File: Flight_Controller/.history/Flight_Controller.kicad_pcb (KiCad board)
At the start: 2 copper layers, 77 parts, among them IC1 AT7456E, J10 USB_C_Receptacle_USB2.0_16P, J11 Conn_ARM_SWD_TagConnect_TC203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, J13 SM06B-GHS-TB, J14 VTX, J6 ESC->FC DSHOT and Telem, J7 ELRS Reciever, J9 Camera, SW1 SW_Push, U1 STM32H743VITx, U2 BMI270, U3 TLV75533PDBV, U4 W25Q128JVSIQ TR, U5 TPS62932, U7 TPD2EUSB30ADRTR, Y2 ABM3-27.000MHZ-D2Y-T

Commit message: Initial Layout Done
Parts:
- removed C10: 33nF, PCM_JLCPCB:C_0603
- removed C12: 6.8pF, PCM_JLCPCB:C_0603
- removed U5: TPS62932, Package_TO_SOT_SMD:SOT-583-8
- added C34: 47uF, PCM_JLCPCB:C_0805, F.Cu at (104.9, 78.5)
- added D6: SMBJ30CA, PCM_JLCPCB:D_SMB, F.Cu at (123.3, 77.5)
- added H1: MountingHole, MountingHole:MountingHole_3.2mm_M3_Pad_Via, F.Cu at (97.4, 53.6)
- added H2: MountingHole, MountingHole:MountingHole_3.2mm_M3_Pad_Via, F.Cu at (127.4, 53.6)
- added H3: MountingHole, MountingHole:MountingHole_3.2mm_M3_Pad_Via, F.Cu at (97.4, 83.6)
- added H4: MountingHole, MountingHole:MountingHole_3.2mm_M3_Pad_Via, F.Cu at (127.4, 83.6)
- added U6: LMR51625XDDCR, Flight_Controller:DDC0006A-MFG, F.Cu at (118.3, 82.1)
- NT1, NT2, NT3, NT4: footprint NetTie:NetTie-2_THT_Pad1.0mm -> NetTie:NetTie-2_SMD_Pad0.5mm
- R7: value 52.3K -> 100kΩ
- R8: value 10kΩ -> 20kΩ
- moved J13 42.5 mm to (121.4, 47.0), turned to 180 degrees
- moved R16 37.3 mm to (122.8, 88.3), turned to 90 degrees
- moved R17 35.4 mm to (96.1, 88.8), turned to -90 degrees
- moved D4 35.3 mm to (120.7, 88.2)
- moved D5 33.4 mm to (98.4, 88.7)
- moved C33 32.8 mm to (121.3, 84.5)
- moved C7 32.4 mm to (123.0, 84.4)
- moved NT1 31.8 mm to (103.0, 52.7), turned to 90 degrees
- moved R5 31.5 mm to (104.8, 55.9), turned to 180 degrees
- moved C17 29.4 mm to (99.9, 88.4)
- moved R4 29.1 mm to (104.8, 54.5), turned to 180 degrees
- moved C2 28.3 mm to (107.7, 57.6), turned to 180 degrees
- moved NT3 27.6 mm to (105.2, 52.6), turned to 90 degrees
- moved J7 27.3 mm to (95.0, 74.5), turned to -90 degrees
- moved C3 26.5 mm to (107.7, 56.2), turned to 180 degrees
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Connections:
- net /Peripherals/Power/3V3_LED renamed /Peripherals/Power/BATT_LED
- net Net-(D1-Pad1) renamed /MCU/Connectors/MCU_LED
- net Net-(D2-Pad1) renamed /MCU/Connectors/USB_LED
- C11 pad 1: /Peripherals/Power/BST -> /Peripherals/Power/CB
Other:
- board outline added: 43.6 x 50 mm

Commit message: Updated Connector Standard
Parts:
- removed D1: Red, PCM_JLCPCB:D_0603
- removed R9: 150Ω, PCM_JLCPCB:R_0603
- added D8: Red, PCM_JLCPCB:D_0603, F.Cu at (127.5, 77.7)
- added R19: 150Ω, PCM_JLCPCB:R_0603, F.Cu at (131.0, 77.7)
- J11: moved to B.Cu
- moved C17 16.0 mm to (101.2, 72.5), turned to 180 degrees
- moved D5 13.6 mm to (101.2, 75.4), turned to 0 degrees
- moved R17 12.2 mm to (99.6, 77.1), turned to 0 degrees
- moved J11 11.0 mm to (123.7, 54.4), turned to 90 degrees
- moved R13 10.8 mm to (94.9, 55.4)
- moved C15 9.54 mm to (102.0, 77.8)
- moved C14 5.17 mm to (104.7, 88.6), turned to 180 degrees
- moved R16 5.00 mm to (127.7, 87.5), turned to 0 degrees
- moved R14 4.64 mm to (98.1, 46.5)
- moved C34 4.36 mm to (104.5, 82.8)
- moved C13 4.29 mm to (104.5, 85.0)
- moved U3 4.28 mm to (104.5, 79.5), turned to 90 degrees
- moved C27 4.06 mm to (100.8, 47.5)
- moved SW1 3.82 mm to (100.7, 45.6)
- moved R8 3.75 mm to (107.5, 78.8), turned to 90 degrees
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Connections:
- J6 pad 7: +BATT -> GND
- J6 pad 8: GND -> +BATT
- U1 pad 46: unconnected-(U1-PB10-Pad46) -> /MCU/Connectors/PB10
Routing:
- added copper zone on F.Cu, net +3V3
- added copper zone on F.Cu, net +5V
- added copper zone on F.Cu, net +BATT
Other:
- board size 43.6 x 50 mm -> 42 x 46 mm
- copper layers 2 -> 4

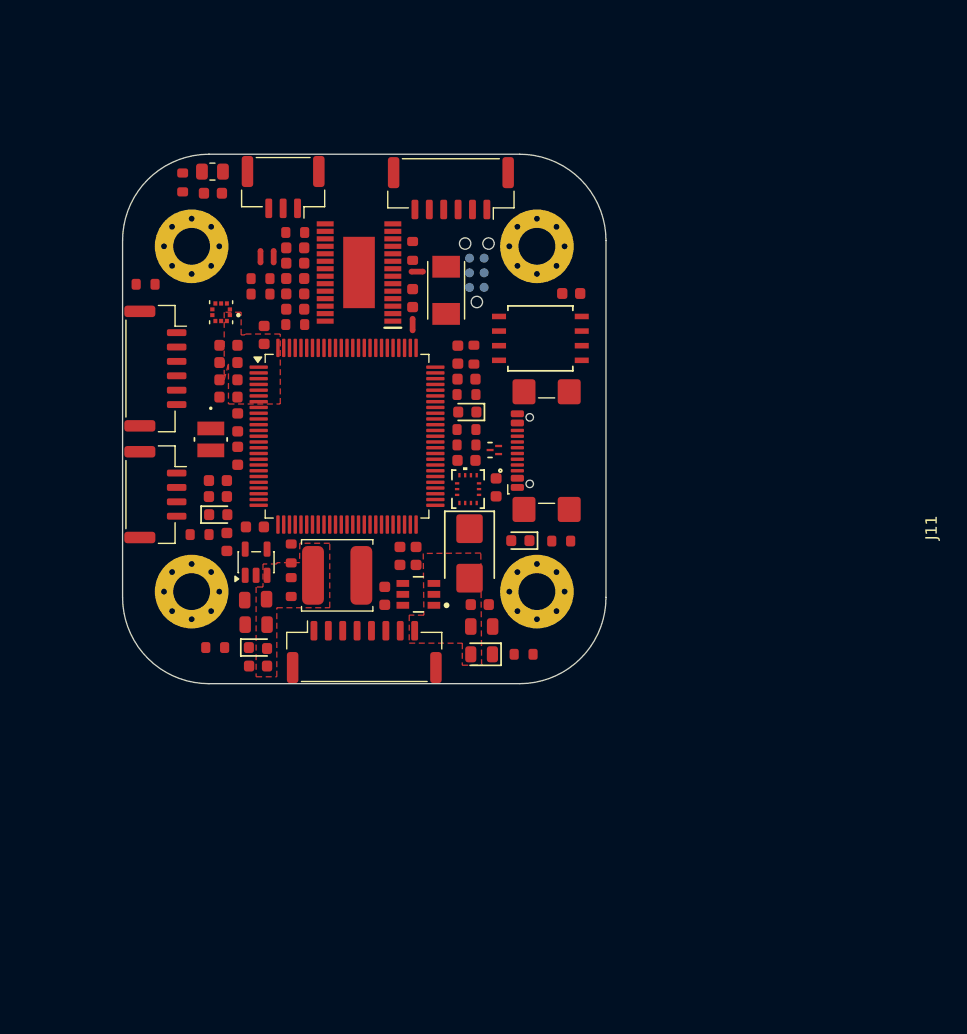
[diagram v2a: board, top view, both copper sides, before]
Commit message: Updated Layout to 60x30
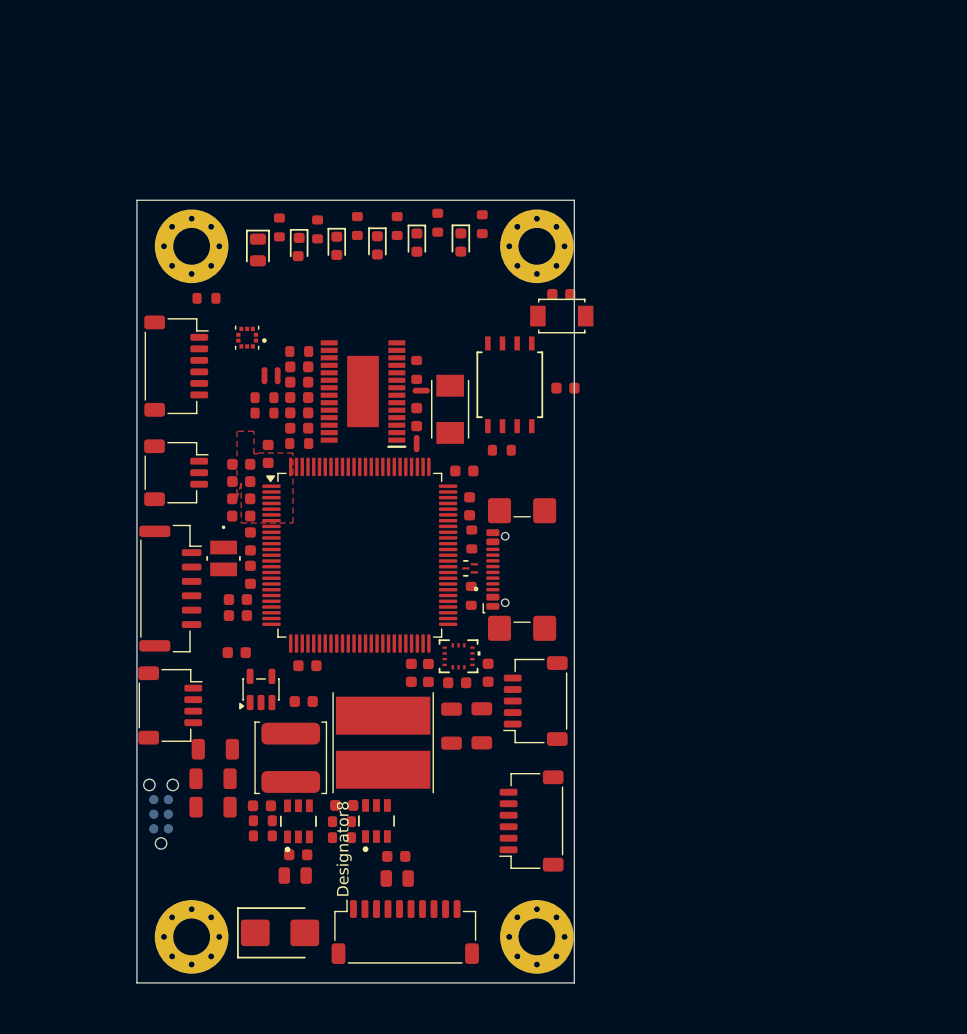
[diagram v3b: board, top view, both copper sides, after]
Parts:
- removed J14: VTX, Connector_JST:JST_GH_SM06B-GHS-TB_1x06-1MP_P1.25mm_Horizontal
- removed J6: ESC->FC DSHOT and Telem, Connector_JST:JST_GH_SM08B-GHS-TB_1x08-1MP_P1.25mm_Horizontal
- added C10: 100nF, PCM_JLCPCB:C_0603, F.Cu at (116.7, 105.1)
- added C12: 100nF, PCM_JLCPCB:C_0603, F.Cu at (112.2, 100.7)
- added C35: 22uF, PCM_JLCPCB:C_1206, F.Cu at (101.0, 95.8)
- added C36: 22uF, PCM_JLCPCB:C_1206, F.Cu at (124.1, 93.8)
- added C37: 22uF, PCM_JLCPCB:C_1206, F.Cu at (121.5, 93.8)
- added C5: 2.2uF, PCM_JLCPCB:C_0805, F.Cu at (116.8, 107.0)
- added D10: White, PCM_JLCPCB:D_0603, F.Cu at (111.5, 52.1)
- added J1: Analog VTX, Connector_JST:JST_SH_SM05B-SRSS-TB_1x05-1MP_P1.00mm_Horizontal, F.Cu at (128.8, 91.6)
- added J2: Digital VTX, Connector_JST:JST_SH_SM06B-SRSS-TB_1x06-1MP_P1.00mm_Horizontal, F.Cu at (128.4, 102.0)
- added J3: GPS+Mag, Connector_JST:JST_SH_SM06B-SRSS-TB_1x06-1MP_P1.00mm_Horizontal, F.Cu at (97.6, 62.5)
- added J4: ESC Connector, Connector_JST:JST_SH_SM10B-SRSS-TB_1x10-1MP_P1.00mm_Horizontal, F.Cu at (117.5, 111.7)
- added L2: 18uH, Inductor_SMD:L_TDK_VLP8040, F.Cu at (115.5, 95.2)
- added R18: 820Ω, PCM_JLCPCB:R_0603, F.Cu at (113.3, 50.3)
- added R9: 100kΩ, PCM_JLCPCB:R_0603, F.Cu at (112.0, 102.1)
- added U8: LMR51625XDDCR, Flight_Controller:DDC0006A-MFG, F.Cu at (115.0, 102.0)
- C13, C34: value 47uF -> 22uF; footprint PCM_JLCPCB:C_0805 -> PCM_JLCPCB:C_1206
- J7: footprint Connector_JST:JST_GH_SM04B-GHS-TB_1x04-1MP_P1.25mm_Horizontal -> Connector_JST:JST_SH_SM04B-SRSS-TB_1x04-1MP_P1.00mm_Horizontal
- J9: footprint Connector_JST:JST_GH_SM03B-GHS-TB_1x03-1MP_P1.25mm_Horizontal -> Connector_JST:JST_SH_SM03B-SRSS-TB_1x03-1MP_P1.00mm_Horizontal
- SW1: footprint Resistor_SMD:R_0805_2012Metric -> Flight_Controller:SW_TS-1088-AR02016
- moved R14 58.6 mm to (112.0, 103.5), turned to 180 degrees
- moved J11 54.5 mm to (96.2, 101.4)
- moved R16 42.7 mm to (106.5, 50.5), turned to 90 degrees
- moved J13 42.5 mm to (97.0, 81.8), turned to -90 degrees
- moved D4 40.1 mm to (104.7, 52.4), turned to -90 degrees
- moved R15 37.4 mm to (109.8, 50.6), turned to 90 degrees
- moved D6 36.8 mm to (106.6, 111.8), turned to 0 degrees
- moved D3 35.0 mm to (108.2, 52.2), turned to -90 degrees
- moved SW1 32.8 mm to (131.1, 58.2), turned to 180 degrees
- moved R17 31.8 mm to (116.8, 50.3), turned to -90 degrees
- moved C27 31.5 mm to (131.0, 56.3), turned to 180 degrees
- moved H3 30.0 mm to (98.9, 112.1)
- moved H4 30.0 mm to (128.9, 112.1)
- moved R19 29.7 mm to (120.3, 50.0), turned to -90 degrees
- moved C16 27.8 mm to (119.5, 89.2), turned to -90 degrees
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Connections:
- net /MCU/Connectors/3V3_LED renamed /MCU/Connectors/MCU_LED
- net /Peripherals/Power/CB renamed /Peripherals/Power/CB_5V
- net /Peripherals/Power/FB renamed /Peripherals/Power/FB_5V
- net /Peripherals/Power/SW renamed /Peripherals/Power/SW_5V
- C1 pad 2: /Peripherals/Power/<NO NET> -> /MCU/Connectors/VIDEO_IN
- J7 pad 2: /MCU/Connectors/ELRS_RX -> GND
- J7 pad 3: /MCU/Connectors/ELRS_TX -> /MCU/Connectors/ELRS_RX
- J7 pad 4: GND -> /MCU/Connectors/ELRS_TX
- J9 pad 2: /Peripherals/Power/<NO NET> -> GND
- J9 pad 3: GND -> /MCU/Connectors/VIDEO_IN
- R14 pad 1: +3V3 -> /Peripherals/Power/FB_9V
- R14 pad 2: /MCU/Connectors/RST_SW -> GND
- R4 pad 1: /Peripherals/Power/<NO NET> -> /MCU/Connectors/VIDEO_IN
- SW1 pad 1: /MCU/Connectors/RST_SW -> GND
- U1 pad 37: unconnected-(U1-PE7-Pad37) -> /MCU/Connectors/DVTX_RX
- U1 pad 38: unconnected-(U1-PE8-Pad38) -> /MCU/Connectors/DVTX_TX
- U1 pad 59: unconnected-(U1-PD12-Pad59) -> /MCU/Connectors/Mag_SCL
- U1 pad 60: unconnected-(U1-PD13-Pad60) -> /MCU/Connectors/Mag_SDA
- U1 pad 61: unconnected-(U1-PD14-Pad61) -> /MCU/Connectors/M5_DSHOT
- U1 pad 62: unconnected-(U1-PD15-Pad62) -> /MCU/Connectors/M6_DSHOT
- U1 pad 64: unconnected-(U1-PC7-Pad64) -> /MCU/Connectors/SBUS
- U1 pad 91: unconnected-(U1-PB5-Pad91) -> /MCU/Connectors/GPS_TX
- U1 pad 92: unconnected-(U1-PB6-Pad92) -> /MCU/Connectors/GPS_RX
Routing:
- removed copper zone on F.Cu, net +5V
- removed copper zone on F.Cu, net +BATT
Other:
- board size 42 x 46 mm -> 38 x 68 mm

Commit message: More Layout Updates
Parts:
- moved R13 9.12 mm to (91.4, 54.1)
- moved J11 4.79 mm to (99.0, 105.4), turned to 180 degrees
- moved J9 2.01 mm to (98.0, 69.8)
- moved J13 1.80 mm to (97.0, 80.0)
- moved J3 1.74 mm to (98.2, 60.9)
- moved C35 0.52 mm to (101.5, 95.8)
- moved C13 0.52 mm to (101.3, 98.4)
- moved C34 0.52 mm to (101.3, 100.8)
- moved C28 0.29 mm to (123.3, 74.7)
- moved R11 0.29 mm to (123.5, 82.5)
- moved R12 0.29 mm to (123.5, 77.6)
- moved U7 0.29 mm to (123.4, 80.1)
- moved J10 0.29 mm to (129.0, 80.2)
- moved XTAL1 0.16 mm to (101.8, 79.2)
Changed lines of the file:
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@@
 		(capping no)
 		(filling no)
-		(grid_origin 113.9 67.1)
+		(grid_origin 113.9 82.1)
 		(pcbplotparams
 			(layerselection 0x00000000_00000000_55555555_5755f5ff)
@@
 	(footprint "Connector_USB:USB_C_Receptacle_GCT_USB4110"
 		(layer "F.Cu")
-		(at 128.75 80.18 90)
+		(at 129.04 80.18 90)
 		(descr "USB 2.0 Type C Receptacle, GCT, 16P, top mounted, horizontal, 5A, https://gct.co/files/drawings/usb4110.pdf")
 		(tags "USB 2.0 C Type-C Receptacle SMD 16P 16C USB4110-GF-A")
@@
 	(footprint "PCM_JLCPCB:R_0603"
 		(layer "F.Cu")
-		(at 123.24 77.57 -90)
+		(at 123.53 77.57 -90)
 		(descr "Resistor SMD 0603 (1608 Metric), square (rectangular) end terminal, IPC_7351 nominal, (Body size source: IPC-SM-782 page 72, https://www.pcb-3d.com/wordpress/wp-content/uploads/ipc-sm-782a_amendment_1_and_2.pdf), generated with kicad-footprint-generator")
 		(tags "resistor")
@@
 	(footprint "Connector_JST:JST_SH_SM06B-SRSS-TB_1x06-1MP_P1.00mm_Horizontal"
 		(layer "F.Cu")
-		(at 97.56 62.51 -90)
+		(at 98.175 60.88 -90)
 		(descr "JST SH series connector, SM06B-SRSS-TB (http://www.jst-mfg.com/product/pdf/eng/eSH.pdf)")
 		(tags "connector JST SH horizontal")
@@
 	(footprint "Flight_Controller:DRT3-L"
 		(layer "F.Cu")
-		(at 123.0899 80.08 90)
+		(at 123.3799 80.08 90)
 		(tags "TPD2EUSB30ADRTR ")
 		(property "Reference" "U7"
@@
 	(footprint "Flight_Controller:XTAL_NX3225GD-8MHZ-STD-CRA-3_NDK-L"
 		(layer "F.Cu")
-		(at 101.675 79.218 -90)
+		(at 101.83 79.218 -90)
 		(tags "NX3225GD-8MHZ-STD-CRA-3 ")
 		(property "Reference" "XTAL1"
@@
 	(footprint "PCM_JLCPCB:R_0603"
 		(layer "F.Cu")
-		(at 123.19 82.47 90)
+		(at 123.48 82.47 90)
 		(descr "Resistor SMD 0603 (1608 Metric), square (rectangular) end terminal, IPC_7351 nominal, (Body size source: IPC-SM-782 page 72, https://www.pcb-3d.com/wordpress/wp-content/uploads/ipc-sm-782a_amendment_1_and_2.pdf), generated with kicad-footprint-generator")
 		(tags "resistor")
@@
 	(footprint "PCM_JLCPCB:R_0603"
 		(layer "F.Cu")
-		(at 100.19 56.62)
+		(at 91.41 54.14)
 		(descr "Resistor SMD 0603 (1608 Metric), square (rectangular) end terminal, IPC_7351 nominal, (Body size source: IPC-SM-782 page 72, https://www.pcb-3d.com/wordpress/wp-content/uploads/ipc-sm-782a_amendment_1_and_2.pdf), generated with kicad-footprint-generator")
 		(tags "resistor")
@@
 	(footprint "PCM_JLCPCB:C_1206"
 		(layer "F.Cu")
-		(at 100.76 98.356926 180)
+		(at 101.28 98.356926 180)
 		(descr "Capacitor SMD 1206 (3216 Metric), square (rectangular) end terminal, IPC_7351 nominal, (Body size source: IPC-SM-782 page 76, https://www.pcb-3d.com/wordpress/wp-content/uploads/ipc-sm-782a_amendment_1_and_2.pdf), generated with kicad-footprint-generator")
 		(tags "capacitor")
@@
 	(footprint "PCM_JLCPCB:C_1206"
 		(layer "F.Cu")
-		(at 100.76 100.83 180)
+		(at 101.28 100.83 180)
 		(descr "Capacitor SMD 1206 (3216 Metric), square (rectangular) end terminal, IPC_7351 nominal, (Body size source: IPC-SM-782 page 76, https://www.pcb-3d.com/wordpress/wp-content/uploads/ipc-sm-782a_amendment_1_and_2.pdf), generated with kicad-footprint-generator")
 		(tags "capacitor")
@@
 	(footprint "Connector_JST:JST_GH_SM06B-GHS-TB_1x06-1MP_P1.25mm_Horizontal"
 		(layer "F.Cu")
-		(at 97.05 81.84 -90)
+		(at 97.05 80.045 -90)
 		(descr "JST GH series connector, SM06B-GHS-TB (http://www.jst-mfg.com/product/pdf/eng/eGH.pdf)")
 		(tags "connector JST GH horizontal")
@@
 	(footprint "PCM_JLCPCB:C_0603"
 		(layer "F.Cu")
-		(at 123.05 74.69 -90)
+		(at 123.34 74.69 -90)
 		(descr "Capacitor SMD 0603 (1608 Metric), square (rectangular) end terminal, IPC_7351 nominal, (Body size source: IPC-SM-782 page 76, https://www.pcb-3d.com/wordpress/wp-content/uploads/ipc-sm-782a_amendment_1_and_2.pdf), generated with kicad-footprint-generator")
 		(tags "capacitor")
@@
 	(footprint "Connector_JST:JST_SH_SM03B-SRSS-TB_1x03-1MP_P1.00mm_Horizontal"
 		(layer "F.Cu")
-		(at 97.55 71.77 -90)
+		(at 98.03 69.82 -90)
 		(descr "JST SH series connector, SM03B-SRSS-TB (http://www.jst-mfg.com/product/pdf/eng/eSH.pdf)")
 		(tags "connector JST SH horizontal")
@@
 	(footprint "PCM_JLCPCB:C_1206"
 		(layer "F.Cu")
-		(at 100.96 95.8 180)
+		(at 101.48 95.8 180)
 		(descr "Capacitor SMD 1206 (3216 Metric), square (rectangular) end terminal, IPC_7351 nominal, (Body size source: IPC-SM-782 page 76, https://www.pcb-3d.com/wordpress/wp-content/uploads/ipc-sm-782a_amendment_1_and_2.pdf), generated with kicad-footprint-generator")
 		(tags "capacitor")
@@
 	(footprint "Connector:Tag-Connect_TC2030-IDC-NL_2x03_P1.27mm_Vertical"
 		(layer "B.Cu")
-		(at 96.245 101.44 90)
+		(at 98.99 105.36 180)
 		(descr "Tag-Connect programming header; http://www.tag-connect.com/Materials/TC2030-IDC-NL.pdf")
 		(tags "tag connect programming header pogo pins")
 		(property "Reference" "J11"
-			(at -22.153 39.497 90)
+			(at -22.153 39.497 0)
 			(layer "F.SilkS")
 			(hide yes)
@@
 		)
 		(property "Value" "Conn_ARM_SWD_TagConnect_TC2030-NL"
-			(at 19.5571 36.483 90)
+			(at 19.5571 36.483 0)
 			(layer "F.Fab")
 			(hide yes)
@@
 		)
 		(property "Datasheet" "https://www.tag-connect.com/wp-content/uploads/bsk-pdf-manager/TC2030-CTX_1.pdf"
-			(at 0 0 270)
+			(at 0 0 0)
 			(unlocked yes)
 			(layer "B.Fab")
@@
 		)
 		(property "Description" "Tag-Connect ARM Cortex SWD JTAG connector, 6 pin, no legs"
-			(at 0 0 270)
+			(at 0 0 0)
 			(unlocked yes)
 			(layer "B.Fab")
@@
 		)
 		(fp_line
-			(start 3.5 -2)
-			(end -3.5 -2)
+			(start 3.5 2)
+			(end 3.5 -2)
 			(stroke
 				(width 0.05)
@@
 		)
 		(fp_line
-			(start -3.5 -2)
-			(end -3.5 2)
+			(start 3.5 -2)
+			(end -3.5 -2)
 			(stroke
 				(width 0.05)
@@
 		)
 		(fp_line
-			(start 3.5 2)
-			(end 3.5 -2)
+			(start -3.5 2)
+			(end 3.5 2)
 			(stroke
 				(width 0.05)
@@
 		)
 		(fp_line
-			(start -3.5 2)
-			(end 3.5 2)
+			(start -3.5 -2)
+			(end -3.5 2)
 			(stroke
 				(width 0.05)
@@
 		)
 		(fp_text user "KEEPOUT"
-			(at -22.153 36.797 90)
+			(at -22.153 36.797 0)
 			(layer "Cmts.User")
 			(effects
@@
 		)
 		(fp_text user "${REFERENCE}"
-			(at -22.153 36.797 90)
+			(at -22.153 36.797 0)
 			(layer "F.Fab")
 			(effects
@@
 		)
 		(pad "" np_thru_hole circle
-			(at -2.54 0 90)
+			(at -2.54 0 180)
 			(size 0.9906 0.9906)
 			(drill 0.9906)
@@
 		)
 		(pad "" np_thru_hole circle
-			(at 2.54 -1.016 90)
+			(at 2.54 -1.016 180)
 			(size 0.9906 0.9906)
 			(drill 0.9906)
@@
 		)
 		(pad "" np_thru_hole circle
-			(at 2.54 1.016 90)
+			(at 2.54 1.016 180)
 			(size 0.9906 0.9906)
 			(drill 0.9906)
@@
 		)
 		(pad "1" connect circle
-			(at -1.27 -0.635 90)
+			(at -1.27 -0.635 180)
 			(size 0.7874 0.7874)
 			(layers "B.Cu" "B.Mask")
@@
 		)
 		(pad "2" connect circle
-			(at -1.27 0.635 90)
+			(at -1.27 0.635 180)
 			(size 0.7874 0.7874)
 			(layers "B.Cu" "B.Mask")
@@
 		)
 		(pad "3" connect circle
-			(at 0 -0.635 90)
+			(at 0 -0.635 180)
 			(size 0.7874 0.7874)
 			(layers "B.Cu" "B.Mask")
@@
 		)
 		(pad "4" connect circle
-			(at 0 0.635 90)
+			(at 0 0.635 180)
 			(size 0.7874 0.7874)
 			(layers "B.Cu" "B.Mask")
@@
 		)
 		(pad "5" connect circle
-			(at 1.27 -0.635 90)
+			(at 1.27 -0.635 180)
 			(size 0.7874 0.7874)
 			(layers "B.Cu" "B.Mask")
@@
 		)
 		(pad "6" connect circle
-			(at 1.27 0.635 90)
+			(at 1.27 0.635 180)
 			(size 0.7874 0.7874)
 			(layers "B.Cu" "B.Mask")
@@
 			(polygon
 				(pts
-					(xy 96.88 100.17) (xy 96.88 102.71) (xy 95.61 102.71) (xy 95.61 100.17)
+					(xy 97.72 104.725) (xy 100.26 104.725) (xy 100.26 105.995) (xy 97.72 105.995)
 				)
 			)
@@
 	)
 	(gr_rect
-		(start 94.15 48.1)
-		(end 132.15 116.1)
+		(start 94.9 48.1)
+		(end 132.9 116.1)
 		(stroke
 			(width 0.05)

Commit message: Almost Done Routing!
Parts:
- R13: moved to B.Cu
- moved R13 26.4 mm to (109.2, 73.7)
- moved A1 10.7 mm to (103.2, 70.7)
- moved SW1 10.4 mm to (140.0, 52.7)
- moved C27 7.70 mm to (138.7, 55.5)
- moved C4 5.79 mm to (128.1, 69.2), turned to 0 degrees
- moved R3 1.94 mm to (118.4, 60.9), turned to -90 degrees
- moved C8 1.91 mm to (104.9, 70.1), turned to 90 degrees
- moved J7 1.74 mm to (98.1, 90.6)
- moved C26 1.72 mm to (103.1, 82.1), turned to 0 degrees
- moved C25 1.27 mm to (103.0, 77.0), turned to 0 degrees
- moved XTAL1 1.19 mm to (103.0, 79.6)
- moved C20 1.18 mm to (121.6, 71.0), turned to 90 degrees
- moved J2 1.09 mm to (129.5, 102.0)
- moved J13 1.08 mm to (98.1, 79.8)
- moved R6 0.90 mm to (125.2, 69.2)
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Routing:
- net +BATT: track 0.00 -> 59.1 mm, vias 0 -> 2
- net /MCU/Connectors/SWCLK: track 0.00 -> 55.7 mm, vias 0 -> 4
- net /MCU/Connectors/VIDEO_OUT: track 0.00 -> 55.5 mm, vias 0 -> 3
- net /MCU/Connectors/SWDIO: track 0.00 -> 51.9 mm, vias 0 -> 4
- net /MCU/Connectors/SWO: track 0.00 -> 49.3 mm, vias 0 -> 4
- net /MCU/Connectors/Mag_SCL: track 0.00 -> 42.5 mm, vias 0 -> 3
- net /MCU/Connectors/Mag_SDA: track 0.00 -> 40.5 mm, vias 0 -> 3
- net /MCU/Connectors/NRST: track 0.00 -> 38.7 mm, vias 0 -> 3
- net /MCU/Connectors/M1_DSHOT: track 0.00 -> 38.6 mm, vias 0 -> 3
- net /MCU/Connectors/ADC_CURR: track 0.00 -> 38.5 mm, vias 0 -> 3
- net +5V: track 0.00 -> 36.9 mm, vias 0 -> 1
- net /MCU/Connectors/M2_DSHOT: track 0.00 -> 35.4 mm, vias 0 -> 3
- net /MCU/Connectors/M3_DSHOT: track 0.00 -> 34.9 mm, vias 0 -> 3
- net /MCU/Connectors/M4_DSHOT: track 0.00 -> 33.9 mm, vias 0 -> 3
- net +3V3: track 0.00 -> 33.1 mm, vias 0 -> 5
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- added copper zone on F.Cu, net +5V
- added copper zone on F.Cu, net +9V
- added copper zone on F.Cu, net +BATT
- added copper zone on F.Cu, net /MCU/Connectors/BB_SPI_CS
- added copper zone on F.Cu, net /MCU/Connectors/OSC_IN
- added copper zone on F.Cu, net /MCU/Connectors/OSC_OUT
- added copper zone on F.Cu, net /MCU/Connectors/OSD_LOS
- added copper zone on F.Cu, net /MCU/Connectors/OSD_VS
- added copper zone on F.Cu, net /Peripherals/Power/FB_5V
- added copper zone on F.Cu, net /Peripherals/Power/FB_9V
- added copper zone on F.Cu, net /Peripherals/Power/SW_5V
- added copper zone on F.Cu, net /Peripherals/Power/SW_9V
- added copper zone on F.Cu, net /Peripherals/Power/VOUT_RES
- added copper zone on F.Cu, net GND
